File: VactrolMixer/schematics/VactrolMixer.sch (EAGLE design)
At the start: 71 parts, among them IC1 NE5532N, IC2 NE5532N, IC6 NE5532N, T1 2N3904, T2 2N3904, T3 2N3904, T4 2N3904

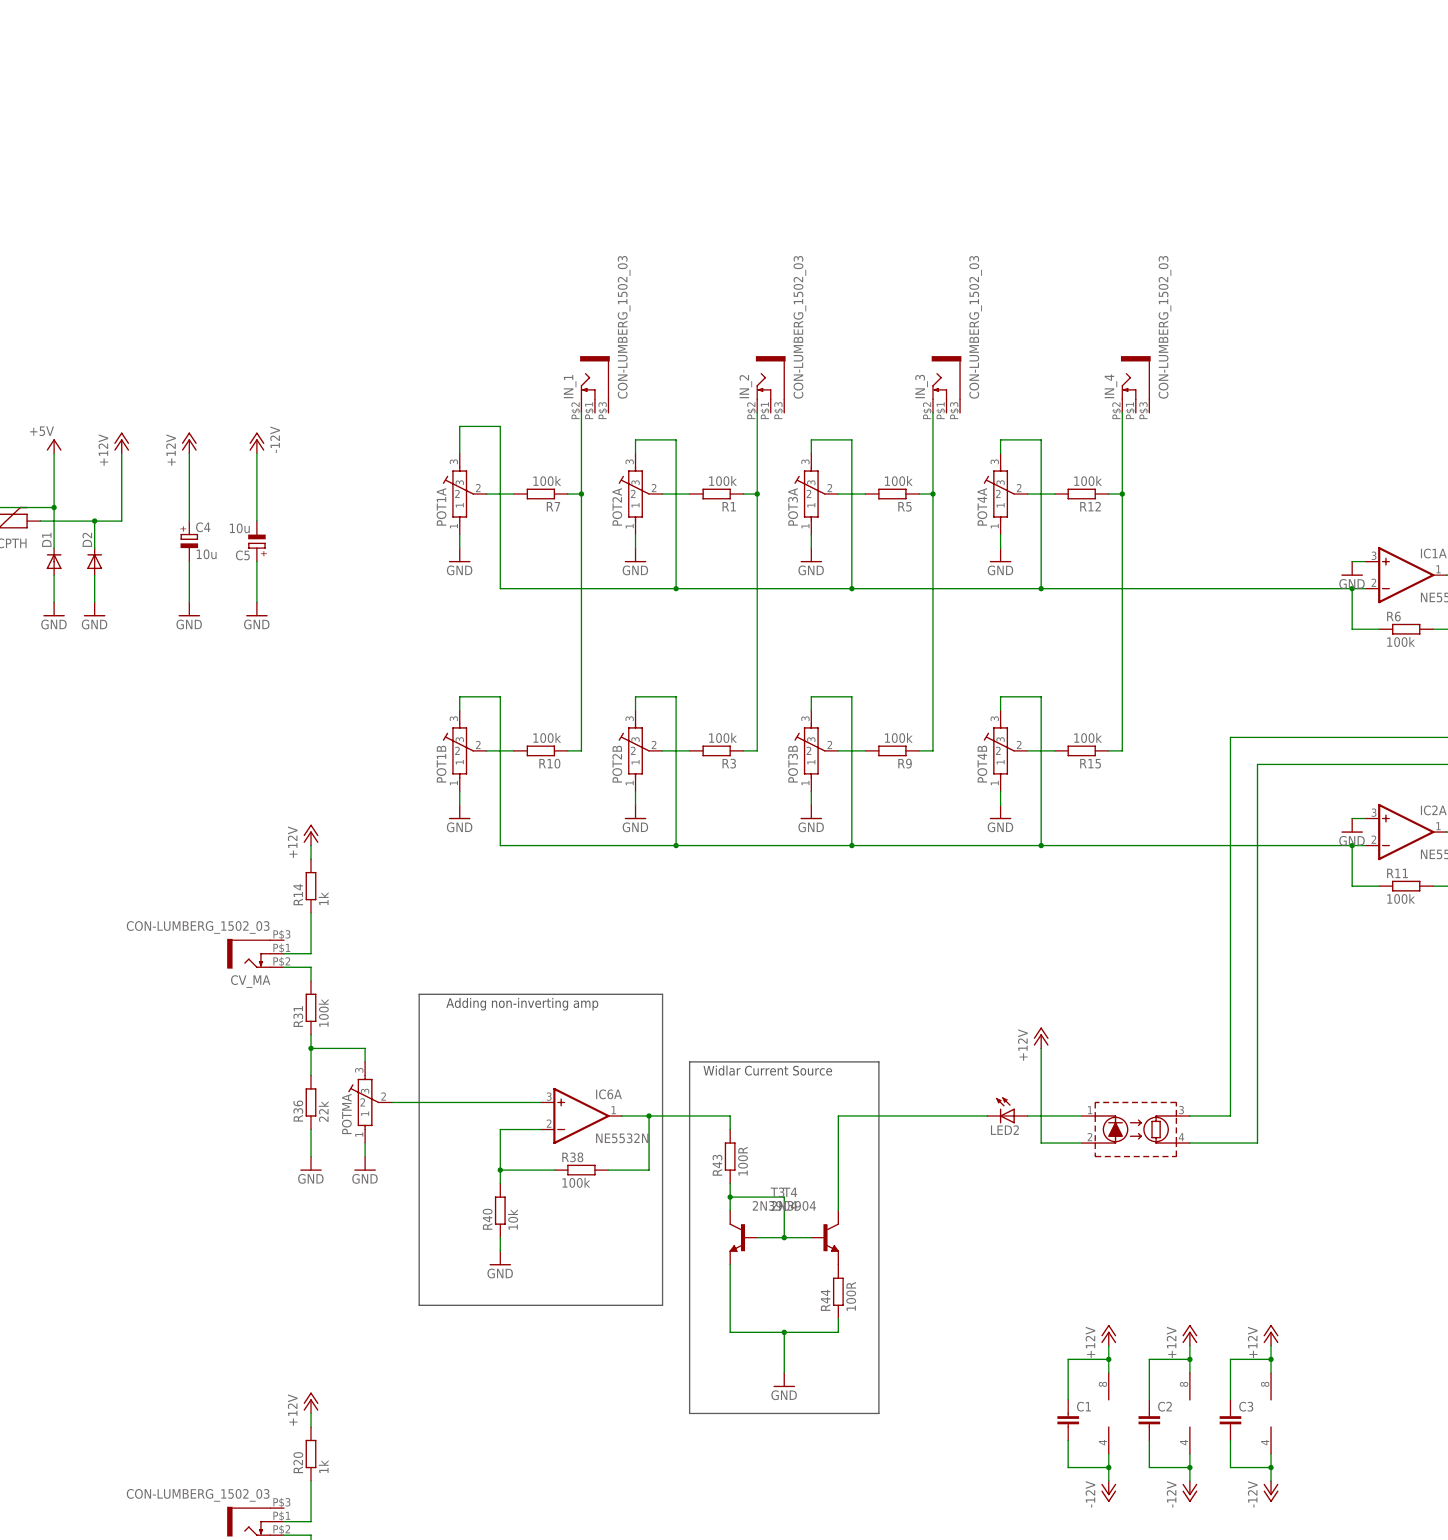
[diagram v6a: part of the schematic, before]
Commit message: added input buffers, changed resistor footprints
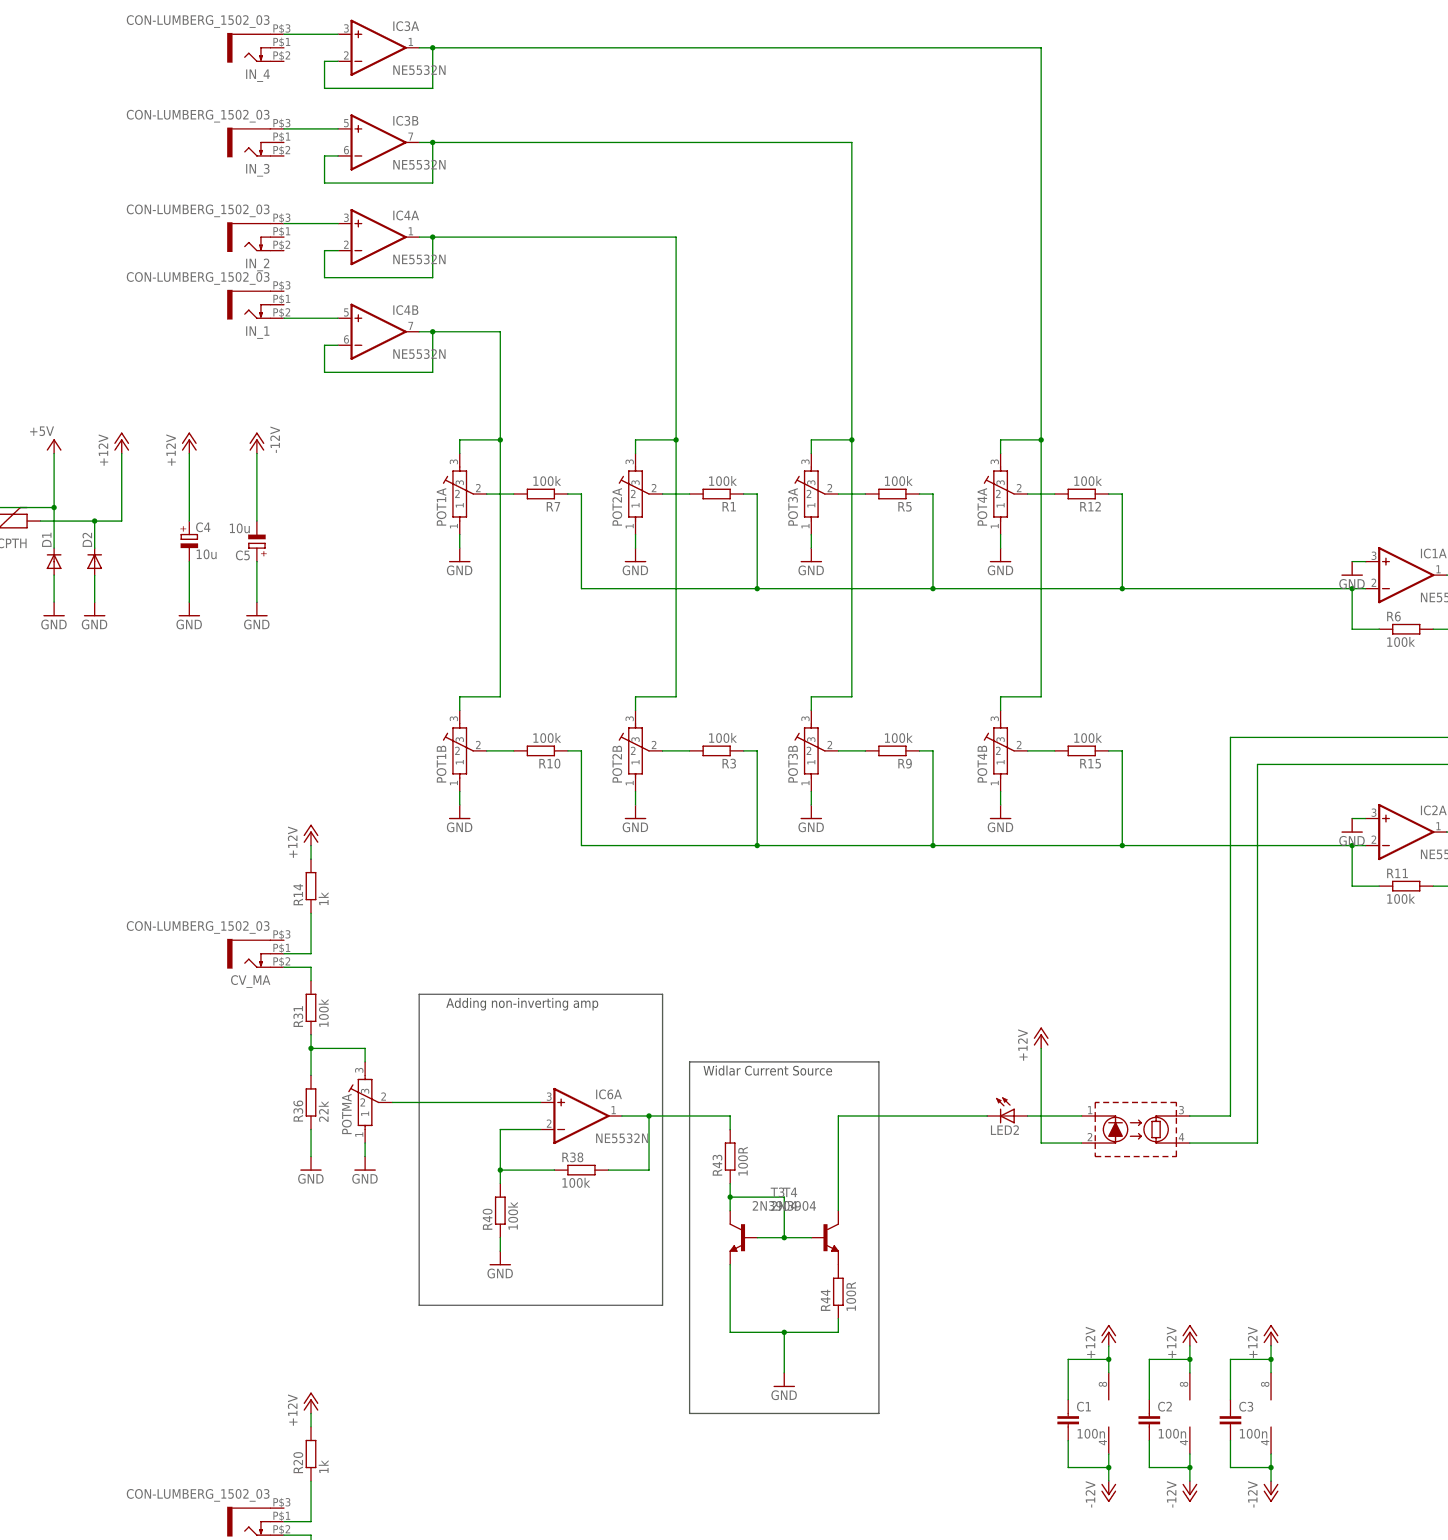
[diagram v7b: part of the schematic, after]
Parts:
- added IC3, IC4: NE5532N, linear:NE5532N
- C1, C2, C3: value (none) -> 100n
- R1, R10, R11, R12, R13, R14, R15, R16, R17, R18, R19, R2, R20, R23, R24, R26, R27, R3, R31, R36, R38, R4, R43, R44, R5, R6, R7, R8, R9: device resistor:R-EU_0411/15 -> Rebel:R-EU_0204/7
- R40: value 10k -> 100k; device resistor:R-EU_0411/15 -> Rebel:R-EU_0204/7
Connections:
- removed net N$37: IN_1.3, R10.1, R7.1
- removed net N$45: IC1A.-IN, POT1AG$1.3, POT2AG$1.3, POT3AG$1.3, POT4AG$1.3, R6.1
- new net N$21: IC4A.-IN, IC4A.OUT, POT2AG$1.3, POT2BG$1.3
- new net N$22: IC4B.+IN, IN_1.3
- new net N$23: IC3A.+IN, IN_4.5
- new net N$24: IC4B.-IN, IC4B.OUT, POT1AG$1.3, POT1BG$1.3
- new net N$53: IC3B.-IN, IC3B.OUT, POT3AG$1.3, POT3BG$1.3
- new net N$58: IC3A.-IN, IC3A.OUT, POT4AG$1.3, POT4BG$1.3
- net N$38: now also IC3B.+IN, IN_3.5; no longer IN_2.3, R1.1, R3.1
- net N$41: now also IC4A.+IN, IN_2.5; no longer IN_3.3, R5.1, R9.1
- net N$46: now also R10.1, R15.1, R3.1, R9.1; no longer POT1BG$1.3, POT2BG$1.3, POT3BG$1.3, POT4BG$1.3
- net N$52: now also IC1A.-IN, R1.1, R5.1, R6.1, R7.1; no longer IN_4.3, R15.1
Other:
- moved on the sheet: IN_1, IN_2, IN_3, IN_4

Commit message: changed jack footprints
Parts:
- CV_MA, CV_MB, IN_1, IN_2, IN_3, IN_4, OUT_A, OUT__B: value CON-LUMBERG_1502_03 -> JACK-PJ-301B; device Rebel:CON-LUMBERG_1502_03 -> Rebel:JACK-PJ-301B
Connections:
- net N$18: now also CV_MA.SW; no longer CV_MA.4
- net N$22: now also IN_1.TIP; no longer IN_1.3
- net N$23: now also IN_4.SLEEVE; no longer IN_4.5
- net N$38: now also IN_3.SLEEVE; no longer IN_3.5
- net N$41: now also IN_2.SLEEVE; no longer IN_2.5
- net N$49: now also CV_MB.TIP; no longer CV_MB.3
- net N$5: now also OUT_A.TIP; no longer OUT_A.3
- net N$51: now also CV_MB.SW; no longer CV_MB.4
- net N$6: now also OUT__B.TIP; no longer OUT__B.3
- net N$7: now also CV_MA.TIP; no longer CV_MA.3
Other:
- moved on the sheet: CV_MA, CV_MB, IN_1, IN_2, IN_3, IN_4, OUT_A, OUT__B
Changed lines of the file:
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@@
 <part name="R11" library="Rebel" deviceset="R-EU_" device="0204/7" value="100k"/>
 <part name="U$2" library="Pingdynasty" deviceset="VTL5C3" device=""/>
-<part name="CV_MA" library="Rebel" deviceset="CON-LUMBERG_1502_03" device=""/>
+<part name="CV_MA" library="Rebel" deviceset="JACK-PJ-301B" device=""/>
 <part name="LED2" library="Rebel" deviceset="LED" device="3MM"/>
 <part name="GND6" library="supply1" deviceset="GND" device=""/>
@@
 <part name="R27" library="Rebel" deviceset="R-EU_" device="0204/7"/>
 <part name="GND17" library="supply1" deviceset="GND" device=""/>
-<part name="OUT_A" library="Rebel" deviceset="CON-LUMBERG_1502_03" device=""/>
-<part name="OUT__B" library="Rebel" deviceset="CON-LUMBERG_1502_03" device=""/>
+<part name="OUT_A" library="Rebel" deviceset="JACK-PJ-301B" device=""/>
+<part name="OUT__B" library="Rebel" deviceset="JACK-PJ-301B" device=""/>
 <part name="R31" library="Rebel" deviceset="R-EU_" device="0204/7" value="100k"/>
 <part name="R1" library="Rebel" deviceset="R-EU_" device="0204/7" value="100k"/>
 <part name="POT2A" library="Rebel" deviceset="POT-ALPS-RK09L" device="1140"/>
-<part name="IN_2" library="Rebel" deviceset="CON-LUMBERG_1502_03" device=""/>
+<part name="IN_2" library="Rebel" deviceset="JACK-PJ-301B" device=""/>
 <part name="R3" library="Rebel" deviceset="R-EU_" device="0204/7" value="100k"/>
 <part name="POT2B" library="Rebel" deviceset="POT-ALPS-RK09L" device="1140"/>
@@
 <part name="R5" library="Rebel" deviceset="R-EU_" device="0204/7" value="100k"/>
 <part name="POT3A" library="Rebel" deviceset="POT-ALPS-RK09L" device="1140"/>
-<part name="IN_3" library="Rebel" deviceset="CON-LUMBERG_1502_03" device=""/>
+<part name="IN_3" library="Rebel" deviceset="JACK-PJ-301B" device=""/>
 <part name="R9" library="Rebel" deviceset="R-EU_" device="0204/7" value="100k"/>
 <part name="POT3B" library="Rebel" deviceset="POT-ALPS-RK09L" device="1140"/>
@@
 <part name="R12" library="Rebel" deviceset="R-EU_" device="0204/7" value="100k"/>
 <part name="POT4A" library="Rebel" deviceset="POT-ALPS-RK09L" device="1140"/>
-<part name="IN_4" library="Rebel" deviceset="CON-LUMBERG_1502_03" device=""/>
+<part name="IN_4" library="Rebel" deviceset="JACK-PJ-301B" device=""/>
 <part name="R15" library="Rebel" deviceset="R-EU_" device="0204/7" value="100k"/>
 <part name="POT4B" library="Rebel" deviceset="POT-ALPS-RK09L" device="1140"/>
@@
 <part name="R7" library="Rebel" deviceset="R-EU_" device="0204/7" value="100k"/>
 <part name="POT1A" library="Rebel" deviceset="POT-ALPS-RK09L" device="1140"/>
-<part name="IN_1" library="Rebel" deviceset="CON-LUMBERG_1502_03" device=""/>
+<part name="IN_1" library="Rebel" deviceset="JACK-PJ-301B" device=""/>
 <part name="R10" library="Rebel" deviceset="R-EU_" device="0204/7" value="100k"/>
 <part name="POT1B" library="Rebel" deviceset="POT-ALPS-RK09L" device="1140"/>
@@
 <part name="C5" library="rcl" deviceset="CPOL-EU" device="E5-6" value="10u"/>
 <part name="R14" library="Rebel" deviceset="R-EU_" device="0204/7" value="1k"/>
-<part name="CV_MB" library="Rebel" deviceset="CON-LUMBERG_1502_03" device=""/>
+<part name="CV_MB" library="Rebel" deviceset="JACK-PJ-301B" device=""/>
 <part name="R16" library="Rebel" deviceset="R-EU_" device="0204/7" value="100k"/>
 <part name="POTMB" library="Rebel" deviceset="POT-ALPS-RK09L" device="1140"/>
@@
 <wire x1="139.7" y1="88.9" x2="144.78" y2="88.9" width="0.1524" layer="91"/>
 <pinref part="R8" gate="G$1" pin="1"/>
-<pinref part="OUT_A" gate="G$1" pin="3"/>
+<pinref part="OUT_A" gate="G$1" pin="TIP"/>
 </segment>
 </net>
@@
 <wire x1="139.7" y1="40.64" x2="144.78" y2="40.64" width="0.1524" layer="91"/>
 <pinref part="R13" gate="G$1" pin="1"/>
-<pinref part="OUT__B" gate="G$1" pin="3"/>
+<pinref part="OUT__B" gate="G$1" pin="TIP"/>
 </segment>
 </net>
@@
 <net name="N$7" class="0">
 <segment>
-<pinref part="CV_MA" gate="G$1" pin="3"/>
+<pinref part="CV_MA" gate="G$1" pin="TIP"/>
 <pinref part="R31" gate="G$1" pin="2"/>
 <wire x1="-154.94" y1="12.7" x2="-149.86" y2="12.7" width="0.1524" layer="91"/>
@@
 <net name="N$18" class="0">
 <segment>
-<pinref part="CV_MA" gate="G$1" pin="4"/>
+<pinref part="CV_MA" gate="G$1" pin="SW"/>
 <wire x1="-154.94" y1="15.24" x2="-149.86" y2="15.24" width="0.1524" layer="91"/>
 <wire x1="-149.86" y1="15.24" x2="-149.86" y2="22.86" width="0.1524" layer="91"/>
@@
 <net name="N$49" class="0">
 <segment>
-<pinref part="CV_MB" gate="G$1" pin="3"/>
+<pinref part="CV_MB" gate="G$1" pin="TIP"/>
 <pinref part="R16" gate="G$1" pin="2"/>
 <wire x1="-154.94" y1="-93.98" x2="-149.86" y2="-93.98" width="0.1524" layer="91"/>
@@
 <net name="N$51" class="0">
 <segment>
-<pinref part="CV_MB" gate="G$1" pin="4"/>
+<pinref part="CV_MB" gate="G$1" pin="SW"/>
 <wire x1="-154.94" y1="-91.44" x2="-149.86" y2="-91.44" width="0.1524" layer="91"/>
 <wire x1="-149.86" y1="-91.44" x2="-149.86" y2="-83.82" width="0.1524" layer="91"/>
@@
 <net name="N$22" class="0">
 <segment>
-<pinref part="IN_1" gate="G$1" pin="3"/>
+<pinref part="IN_1" gate="G$1" pin="TIP"/>
 <pinref part="IC4" gate="B" pin="+IN"/>
 <wire x1="-154.94" y1="134.62" x2="-144.78" y2="134.62" width="0.1524" layer="91"/>
@@
 <net name="N$23" class="0">
 <segment>
-<pinref part="IN_4" gate="G$1" pin="5"/>
+<pinref part="IN_4" gate="G$1" pin="SLEEVE"/>
 <pinref part="IC3" gate="A" pin="+IN"/>
 <wire x1="-154.94" y1="187.96" x2="-144.78" y2="187.96" width="0.1524" layer="91"/>
@@
 <segment>
 <pinref part="IC3" gate="B" pin="+IN"/>
-<pinref part="IN_3" gate="G$1" pin="5"/>
+<pinref part="IN_3" gate="G$1" pin="SLEEVE"/>
 <wire x1="-144.78" y1="170.18" x2="-154.94" y2="170.18" width="0.1524" layer="91"/>
 </segment>
@@
 <segment>
 <pinref part="IC4" gate="A" pin="+IN"/>
-<pinref part="IN_2" gate="G$1" pin="5"/>
+<pinref part="IN_2" gate="G$1" pin="SLEEVE"/>
 <wire x1="-144.78" y1="152.4" x2="-154.94" y2="152.4" width="0.1524" layer="91"/>
 </segment>
